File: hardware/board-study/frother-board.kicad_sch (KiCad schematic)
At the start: 9 parts, among them U1 unmarked

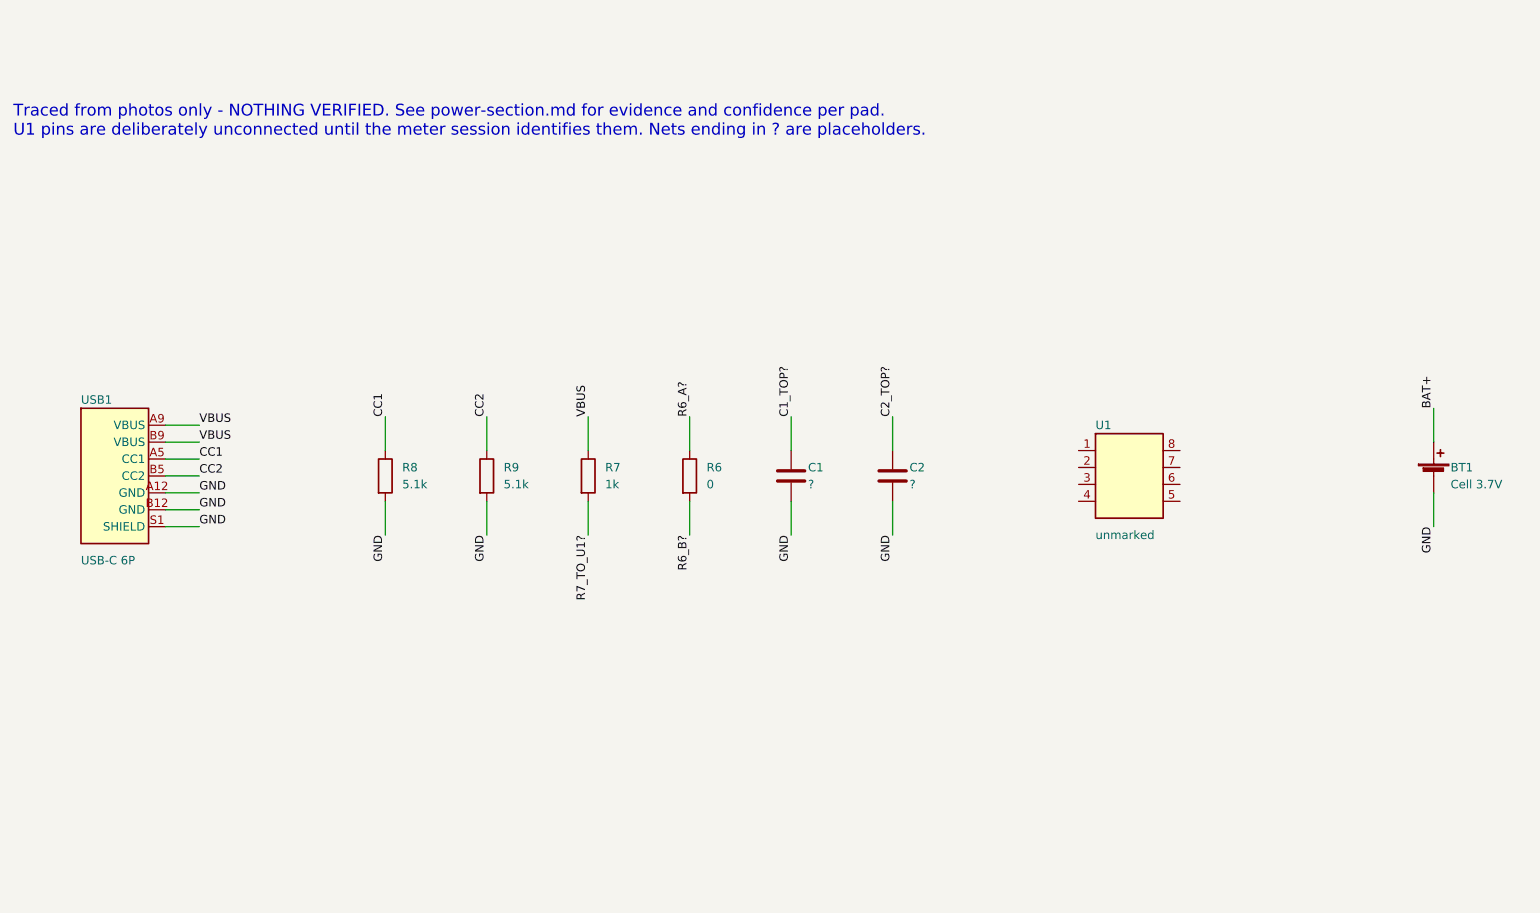
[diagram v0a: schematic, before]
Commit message: Board study: review fixes for the power section
- Confidence now covers the net name, not just the trace: CC and R7
  rows downgraded to inferred; cite both photos
- C1/C2 tied to U1 pins 2/1 as inferred (pads adjacent, trace unseen)
- R7 (1 kOhm) can't be the charging path; hypotheses reworded as
  predictions, glossary wording (no "controller"/"shell tabs")
- List R1-R5 and C4 as parts not yet assigned to a section
- Meter checklist starts by confirming the U1 pin-1 call
- check_netlist.py: clear error when a section has no Connections table

Refs #9

Co-Authored-By: Claude Opus 5.5 (1M context) <noreply@anthropic.com>
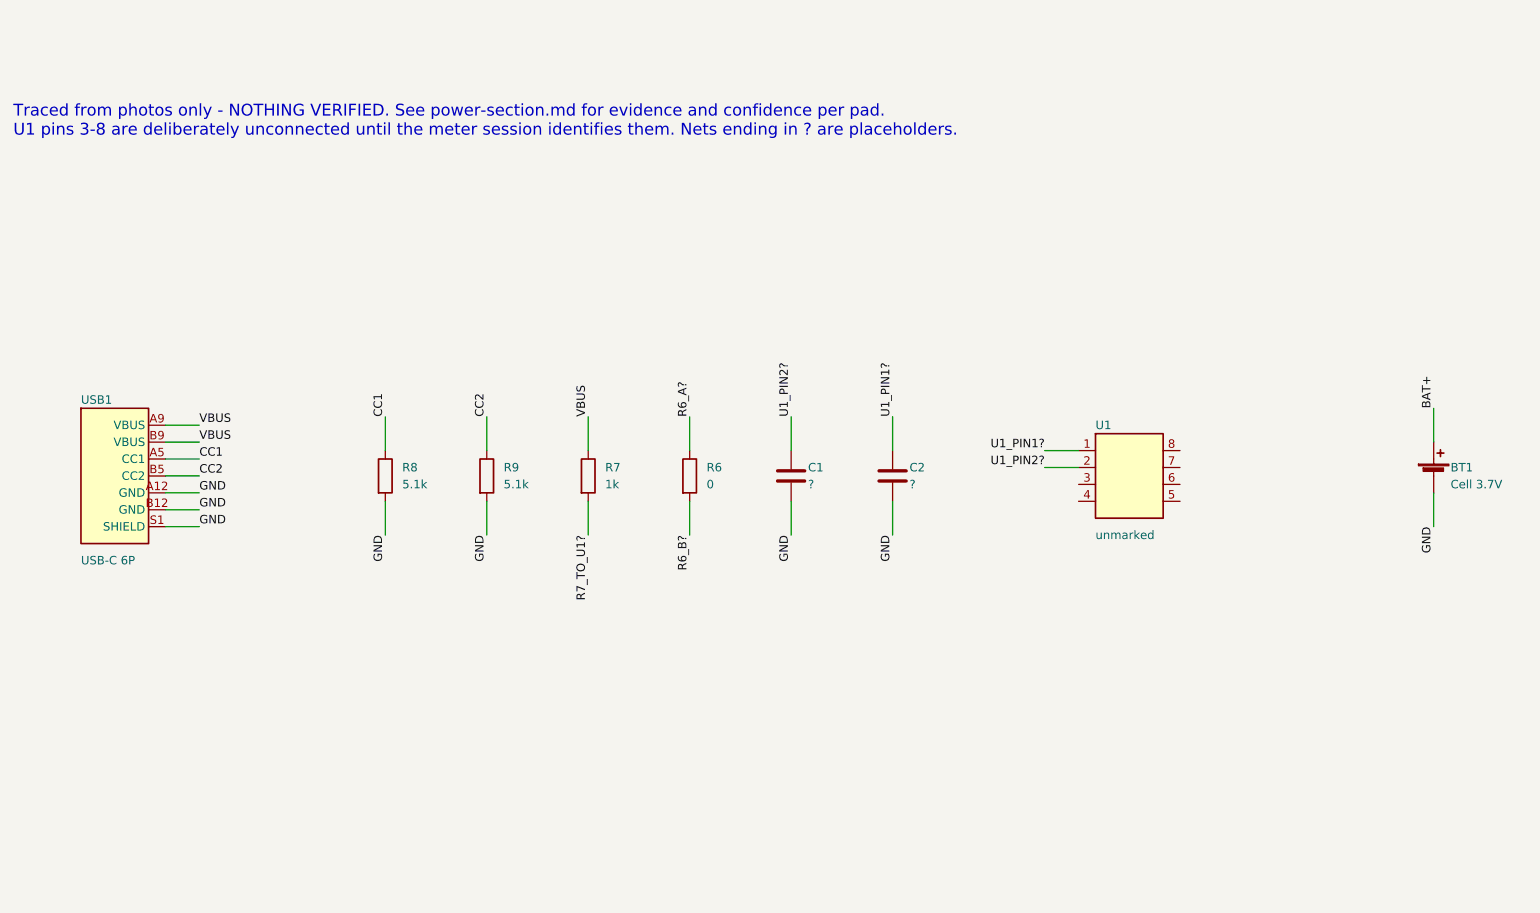
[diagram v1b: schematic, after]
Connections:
- net C1_TOP? is gone; now on net U1_PIN2?: C1.1
- net C2_TOP? is gone; now on net U1_PIN1?: C2.1
- net U1_PIN1?: now reaches U1.1
- net U1_PIN2?: now reaches U1.2
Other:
- note added: "Traced from photos only - NOTHING VERIFIED. See power-section.md for evidence and confidence per pad. U1 pins 3-8 are deliberately unconnected until the meter session identifies them. Nets ending in ? are placeholders."
- note removed: "Traced from photos only - NOTHING VERIFIED. See power-section.md for evidence and confidence per pad. U1 pins are deliberately unconnected until the meter session identifies them. Nets ending in ? are placeholders."
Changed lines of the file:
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@@
     (pin "1") (pin "2"))
   (wire (pts (xy 147.32 97.79) (xy 147.32 92.71)) (stroke (width 0) (type default) (color 0 0 0 0)))
-  (label "C1_TOP?" (at 147.32 92.71 90) (effects (font (size 1.27 1.27)) (justify left bottom)))
+  (label "U1_PIN2?" (at 147.32 92.71 90) (effects (font (size 1.27 1.27)) (justify left bottom)))
   (wire (pts (xy 147.32 105.41) (xy 147.32 110.49)) (stroke (width 0) (type default) (color 0 0 0 0)))
   (label "GND" (at 147.32 110.49 270) (effects (font (size 1.27 1.27)) (justify right bottom)))
@@
     (pin "1") (pin "2"))
   (wire (pts (xy 162.56 97.79) (xy 162.56 92.71)) (stroke (width 0) (type default) (color 0 0 0 0)))
-  (label "C2_TOP?" (at 162.56 92.71 90) (effects (font (size 1.27 1.27)) (justify left bottom)))
+  (label "U1_PIN1?" (at 162.56 92.71 90) (effects (font (size 1.27 1.27)) (justify left bottom)))
   (wire (pts (xy 162.56 105.41) (xy 162.56 110.49)) (stroke (width 0) (type default) (color 0 0 0 0)))
   (label "GND" (at 162.56 110.49 270) (effects (font (size 1.27 1.27)) (justify right bottom)))
@@
     (property "Datasheet" "" (id 3) (at 198.12 101.6 0) (effects (font (size 1.27 1.27)) hide))
     (pin "1") (pin "2") (pin "3") (pin "4") (pin "5") (pin "6") (pin "7") (pin "8"))
+  (wire (pts (xy 190.5 97.79) (xy 185.42 97.79)) (stroke (width 0) (type default) (color 0 0 0 0)))
+  (label "U1_PIN1?" (at 185.42 97.79 180) (effects (font (size 1.27 1.27)) (justify right bottom)))
+  (wire (pts (xy 190.5 100.33) (xy 185.42 100.33)) (stroke (width 0) (type default) (color 0 0 0 0)))
+  (label "U1_PIN2?" (at 185.42 100.33 180) (effects (font (size 1.27 1.27)) (justify right bottom)))
   (symbol (lib_id "Device:Battery_Cell") (at 243.84 101.6 0) (unit 1)
     (in_bom yes) (on_board yes) (fields_autoplaced)
@@
   (wire (pts (xy 243.84 104.14) (xy 243.84 109.22)) (stroke (width 0) (type default) (color 0 0 0 0)))
   (label "GND" (at 243.84 109.22 270) (effects (font (size 1.27 1.27)) (justify right bottom)))
-  (text "Traced from photos only - NOTHING VERIFIED. See power-section.md for evidence and confidence per pad.\nU1 pins are deliberately unconnected until the meter session identifies them. Nets ending in ? are placeholders." (at 30.48 50.8 0) (effects (font (size 1.778 1.778)) (justify left bottom)))
+  (text "Traced from photos only - NOTHING VERIFIED. See power-section.md for evidence and confidence per pad.\nU1 pins 3-8 are deliberately unconnected until the meter session identifies them. Nets ending in ? are placeholders." (at 30.48 50.8 0) (effects (font (size 1.778 1.778)) (justify left bottom)))
   (sheet_instances
     (path "/" (page "1"))
   )
   (symbol_instances
-    (path "/fe5824a8-6951-4246-85b3-69035b018632" (reference "USB1") (unit 1) (value "USB-C 6P") (footprint ""))
-    (path "/6d23e011-6856-4467-8b8d-bd364b8eccce" (reference "R8") (unit 1) (value "5.1k") (footprint ""))
-    (path "/3e40a0d3-60bb-4790-afe1-f46d8e64952d" (reference "R9") (unit 1) (value "5.1k") (footprint ""))
-    (path "/8814d5a4-62ad-4df4-b29d-7ae18a54b580" (reference "R7") (unit 1) (value "1k") (footprint ""))
-    (path "/61e547ac-15e9-40c6-8bcc-f09cbb4f4943" (reference "R6") (unit 1) (value "0") (footprint ""))
-    (path "/3ebf5558-1b0f-4231-8370-bbaccc1c2201" (reference "C1") (unit 1) (value "?") (footprint ""))
-    (path "/2bfee61e-4933-46da-b8eb-aa675dcc9958" (reference "C2") (unit 1) (value "?") (footprint ""))
-    (path "/b15a8f38-9b0c-4949-a41f-a2b18a36a1d2" (reference "U1") (unit 1) (value "unmarked") (footprint ""))
-    (path "/cca0f802-088d-4732-874e-672200a0e317" (reference "BT1") (unit 1) (value "Cell 3.7V") (footprint ""))
+    (path "/7375f5b2-7019-43dc-a7a7-9c2191542587" (reference "USB1") (unit 1) (value "USB-C 6P") (footprint ""))
+    (path "/8fb701c3-37cd-402d-8132-13d60b9b7852" (reference "R8") (unit 1) (value "5.1k") (footprint ""))
+    (path "/555120e3-b096-4aa1-975e-d214ecb7fdff" (reference "R9") (unit 1) (value "5.1k") (footprint ""))
+    (path "/c3a9b027-8a85-478c-b6ec-1f5a1443d2bc" (reference "R7") (unit 1) (value "1k") (footprint ""))
+    (path "/3653792a-1dfb-414b-9a5b-3158c8579d5e" (reference "R6") (unit 1) (value "0") (footprint ""))
+    (path "/0cdbd99f-aba2-4f8c-9c4a-e3b90fb3b251" (reference "C1") (unit 1) (value "?") (footprint ""))
+    (path "/4b24d584-5984-4a9c-a9b4-b6423efba54e" (reference "C2") (unit 1) (value "?") (footprint ""))
+    (path "/e169dbd4-c22f-4101-9484-d0ed5a35dc6b" (reference "U1") (unit 1) (value "unmarked") (footprint ""))
+    (path "/e2356215-7576-4fc3-8ee8-865a624baa7e" (reference "BT1") (unit 1) (value "Cell 3.7V") (footprint ""))
   )
 )

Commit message: Board study: draft Motor drive and button/LED sections
Every part on the front of the Board is now in the schematic.
Traced from photos only; nothing verified yet.

- motor-section.md: Motor, D2, C3; low-side switching, flyback and
  noise-suppression hypotheses; meter checklist incl. D2 polarity
- button-led-section.md: K1, LED1-4, R1, R3, R5; panel-window-to-LED
  mapping from position; LED nets untraced; charlieplexing hypothesis
- R2, C4, R4 drawn as unassigned
- check_netlist.py: checks every *-section.md; "—" means untraced

Refs #10, #11

Co-Authored-By: Claude Opus 5.5 (1M context) <noreply@anthropic.com>
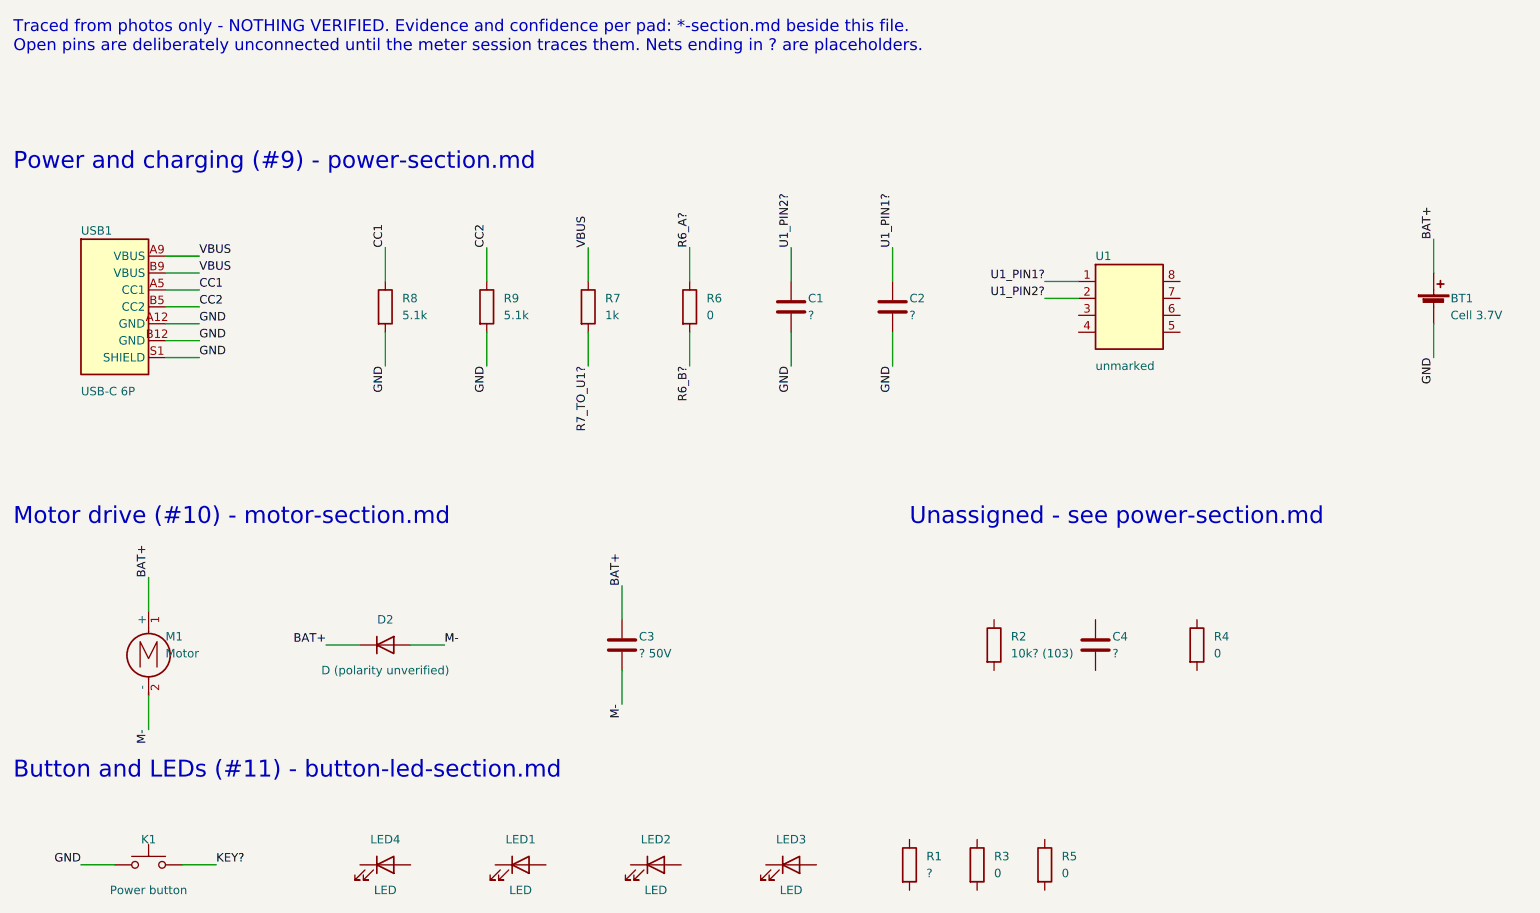
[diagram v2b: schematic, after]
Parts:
- added C3: ? 50V, symbol Device:C
- added C4: ?, symbol Device:C
- added D2: D (polarity unverified), symbol Device:D
- added K1: Power button, symbol Switch:SW_Push
- added LED1, LED2, LED3, LED4: LED, symbol Device:LED
- added M1: Motor, symbol Motor:Motor_DC
- added R1: ?, symbol Device:R
- added R2: 10k? (103), symbol Device:R
- added R3, R4, R5: 0, symbol Device:R
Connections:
- net BAT+: now also C3.1, D2.1 (K), M1.1 (+)
- net GND: now also K1.1
- new net KEY?: K1.2
- new net M-: C3.2, D2.2 (A), M1.2 (-)
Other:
- note added: "Button and LEDs (#11) - button-led-section.md"
- note added: "Motor drive (#10) - motor-section.md"
- note added: "Power and charging (#9) - power-section.md"
- note added: "Traced from photos only - NOTHING VERIFIED. Evidence and confidence per pad: *-section.md beside this file. Open pins are deliberately unconnected until the meter session traces them. Nets ending in ? are placeholders."
- note added: "Unassigned - see power-section.md"
- note removed: "Traced from photos only - NOTHING VERIFIED. See power-section.md for evidence and confidence per pad. U1 pins 3-8 are deliberately unconnected until the meter session identifies them. Nets ending in ? are placeholders."
